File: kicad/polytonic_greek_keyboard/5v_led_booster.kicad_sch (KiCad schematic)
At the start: 2 parts

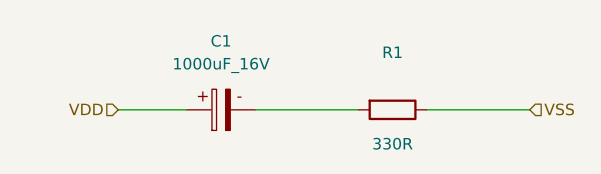
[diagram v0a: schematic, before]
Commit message: [ADD] an initial matrix of what the keyboard will look like logically
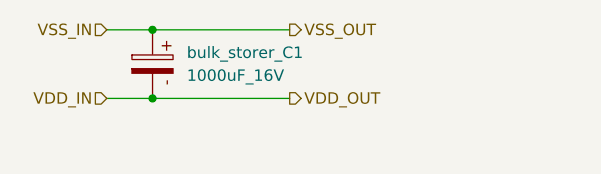
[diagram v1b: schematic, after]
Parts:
- removed R1: 330R_0603, PCM_Resistor_SMD_AKL:R_0603_1608Metric_Pad1.05x0.95mm_HandSolder, symbol PCM_4ms_Resistor:330R_0603
- renumbered C1 to bulk_storer_C1
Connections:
- net VDD_IN: now reaches bulk_storer_C1.2
- net VDD renamed VSS_IN
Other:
- moved on the sheet: bulk_storer_C1
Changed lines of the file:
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@@
 	(generator_version "9.0")
 	(paper "A4")
+	(junction
+		(at 26.67 13.97)
+		(diameter 0)
+		(color 0 0 0 0)
+	)
+	(junction
+		(at 26.67 21.59)
+		(diameter 0)
+		(color 0 0 0 0)
+	)
 	(wire
 		(pts
-			(xy 30.48 22.86) (xy 22.86 22.86)
+			(xy 21.59 21.59) (xy 26.67 21.59)
 		)
 		(stroke
@@
 	(wire
 		(pts
-			(xy 68.58 22.86) (xy 57.15 22.86)
+			(xy 26.67 21.59) (xy 41.91 21.59)
 		)
 		(stroke
@@
 	(wire
 		(pts
-			(xy 49.53 22.86) (xy 38.1 22.86)
+			(xy 26.67 13.97) (xy 41.91 13.97)
 		)
 		(stroke
@@
 		)
 	)
-	(hierarchical_label "VSS"
-		(shape input)
-		(at 68.58 22.86 0)
+	(wire
+		(pts
+			(xy 21.59 13.97) (xy 26.67 13.97)
+		)
+		(stroke
+			(width 0)
+			(type default)
+		)
+	)
+	(hierarchical_label "VSS_OUT"
+		(shape output)
+		(at 41.91 13.97 0)
 		(effects
 			(font
@@
 		)
 	)
-	(hierarchical_label "VDD"
+	(hierarchical_label "VSS_IN"
 		(shape input)
-		(at 22.86 22.86 180)
+		(at 21.59 13.97 180)
 		(effects
 			(font
@@
 		)
 	)
-	(symbol
-		(lib_id "PCM_4ms_Resistor:330R_0603")
-		(at 53.34 22.86 270)
-		(unit 1)
-		(exclude_from_sim no)
-		(in_bom yes)
-		(on_board yes)
-		(dnp no)
-		(property "Reference" "R1"
-			(at 53.34 16.51 90)
-			(effects
-				(font
-					(size 1.27 1.27)
-				)
+	(hierarchical_label "VDD_IN"
+		(shape input)
+		(at 21.59 21.59 180)
+		(effects
+			(font
+				(size 1.27 1.27)
 			)
+			(justify right)
 		)
-		(property "Value" "330R_0603"
-			(at 53.34 20.32 90)
-			(effects
-				(font
-					(size 1.27 1.27)
-				)
-				(hide yes)
+	)
+	(hierarchical_label "VDD_OUT"
+		(shape output)
+		(at 41.91 21.59 0)
+		(effects
+			(font
+				(size 1.27 1.27)
 			)
-		)
-		(property "Footprint" "PCM_Resistor_SMD_AKL:R_0603_1608Metric_Pad1.05x0.95mm_HandSolder"
-			(at 40.64 20.32 0)
-			(effects
-				(font
-					(size 1.27 1.27)
-				)
-				(justify left)
-				(hide yes)
-			)
-		)
-		(property "Datasheet" ""
-			(at 53.34 22.86 0)
-			(effects
-				(font
-					(size 1.27 1.27)
-				)
-				(hide yes)
-			)
-		)
-		(property "Description" "330R, 1%, 1/10W, 0603"
-			(at 53.34 22.86 0)
-			(effects
-				(font
-					(size 1.27 1.27)
-				)
-				(hide yes)
-			)
-		)
-		(property "Specifications" "330R, 1%, 1/10W, 0603"
-			(at 45.466 20.32 0)
-			(effects
-				(font
-					(size 1.27 1.27)
-				)
-				(justify left)
-				(hide yes)
-			)
-		)
-		(property "Manufacturer" "Yageo"
-			(at 43.942 20.32 0)
-			(effects
-				(font
-					(size 1.27 1.27)
-				)
-				(justify left)
-				(hide yes)
-			)
-		)
-		(property "Part Number" "RC0603FR-07330RL"
-			(at 42.418 20.32 0)
-			(effects
-				(font
-					(size 1.27 1.27)
-				)
-				(justify left)
-				(hide yes)
-			)
-		)
-		(property "Display" "330R"
-			(at 53.34 26.67 90)
-			(effects
-				(font
-					(size 1.27 1.27)
-				)
-			)
-		)
-		(property "JLCPCB ID" "C23138"
-			(at 38.1 24.13 0)
-			(effects
-				(font
-					(size 1.27 1.27)
-				)
-				(hide yes)
-			)
-		)
-		(pin "2"
-		)
-		(pin "1"
-		)
-		(instances
-			(project ""
-				(path "/cbe25a1b-6c02-43c2-9ff9-ba274c7cf6a2/e41612ad-bc28-4c90-9b22-fd29a2764a15"
-					(reference "R1")
-					(unit 1)
-				)
-			)
+			(justify left)
 		)
 	)
 	(symbol
 		(lib_id "PCM_SL_Capacitors:1000uF_16V")
-		(at 34.29 22.86 0)
+		(at 26.67 17.78 270)
 		(unit 1)
 		(exclude_from_sim no)
@@
 		(dnp no)
 		(fields_autoplaced yes)
-		(property "Reference" "C1"
-			(at 34.29 15.24 0)
+		(property "Reference" "bulk_storer_C1"
+			(at 30.48 16.5099 90)
 			(effects
 				(font
 					(size 1.27 1.27)
 				)
+				(justify left)
 			)
 		)
 		(property "Value" "1000uF_16V"
-			(at 34.29 17.78 0)
+			(at 30.48 19.0499 90)
 			(effects
 				(font
 					(size 1.27 1.27)
 				)
+				(justify left)
 			)
 		)
 		(property "Footprint" "Capacitor_THT:CP_Radial_D10.0mm_P5.00mm"
-			(at 35.052 26.67 0)
+			(at 22.86 18.542 0)
 			(effects
 				(font
@@
 		)
 		(property "Datasheet" ""
-			(at 34.798 22.86 0)
+			(at 26.67 18.288 0)
 			(effects
 				(font
@@
 		)
 		(property "Description" "1000uF, 16V Electrolytic Capacitor"
-			(at 34.29 22.86 0)
+			(at 26.67 17.78 0)
 			(effects
 				(font
@@
 		)
 		(instances
-			(project ""
-				(path "/cbe25a1b-6c02-43c2-9ff9-ba274c7cf6a2/e41612ad-bc28-4c90-9b22-fd29a2764a15"
-					(reference "C1")
+			(project "polytonic_greek_keyboard"
+				(path "/cbe25a1b-6c02-43c2-9ff9-ba274c7cf6a2/09ff75ff-3c8b-43b7-a704-ac023cbe9eff/57a20682-d779-4340-9769-ea32ac8b4a87"
+					(reference "bulk_storer_C1")
 					(unit 1)
 				)

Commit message: [UPDATE] the final merged version of the schematic before splitting into two separate kicad projects
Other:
- company: (none) -> Henry's Software House
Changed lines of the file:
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@@
 	(generator_version "9.0")
 	(paper "A4")
+	(title_block
+		(rev "1 - do not edit connector pin layout.")
+		(company "Henry's Software House")
+	)
 	(junction
 		(at 26.67 13.97)
